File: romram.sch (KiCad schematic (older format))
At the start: 8 parts, among them U10 HM62256BLP, U6 28C64, U7 28C64, U8 HM6264, U9 HM6264

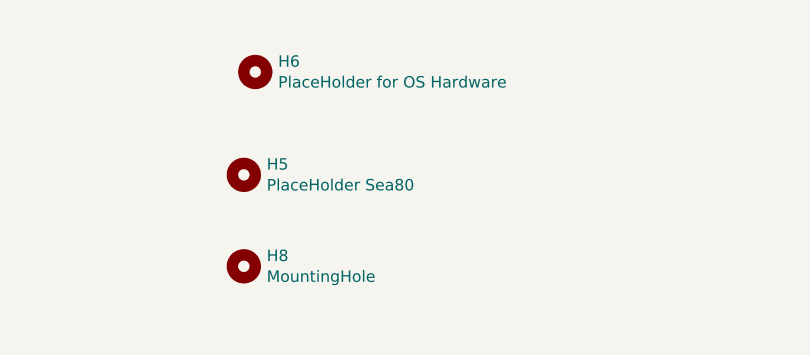
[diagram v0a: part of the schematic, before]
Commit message: Board rerouted. Missing Creative commons
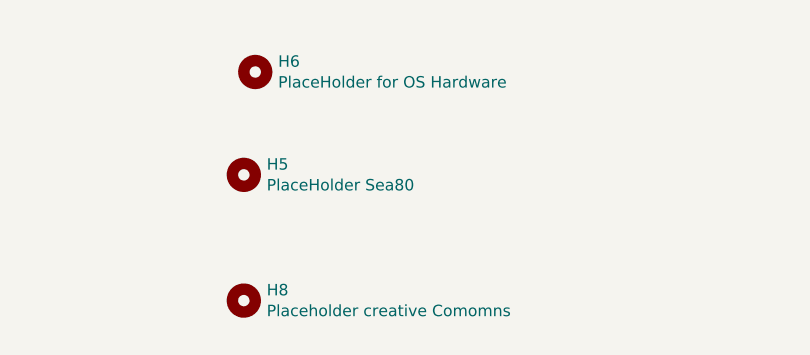
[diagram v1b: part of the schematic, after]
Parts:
- H8: value MountingHole -> Placeholder creative Comomns
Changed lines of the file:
@@
 $Comp
 L Mechanical:MountingHole H8
-U 1 1 6059FCB2
-P 2250 6800
-F 0 "H8" H 2350 6846 50  0000 L CNN
-F 1 "MountingHole" H 2350 6755 50  0000 L CNN
-F 2 "" H 2250 6800 50  0001 C CNN
-F 3 "~" H 2250 6800 50  0001 C CNN
-	1    2250 6800
+U 1 1 60AAEE1C
+P 2250 6950
+F 0 "H8" H 2350 6996 50  0000 L CNN
+F 1 "Placeholder creative Comomns" H 2350 6905 50  0000 L CNN
+F 2 "" H 2250 6950 50  0001 C CNN
+F 3 "~" H 2250 6950 50  0001 C CNN
+	1    2250 6950
 	1    0    0    -1
 $EndComp
